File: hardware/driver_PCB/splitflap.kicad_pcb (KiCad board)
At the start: 2 copper layers, 111.8 x 95.2 mm, 19 parts, among them IC1 CD4049UBE, IC2 CD4049UBE, J1 Conn_01x02_Male, J2 Conn_01x08_Male, J3 Conn_01x16_Female, U1 74HC595, U2 74HC595, U3 SN754410NE, U4 SN754410NE, U5 SN754410NE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

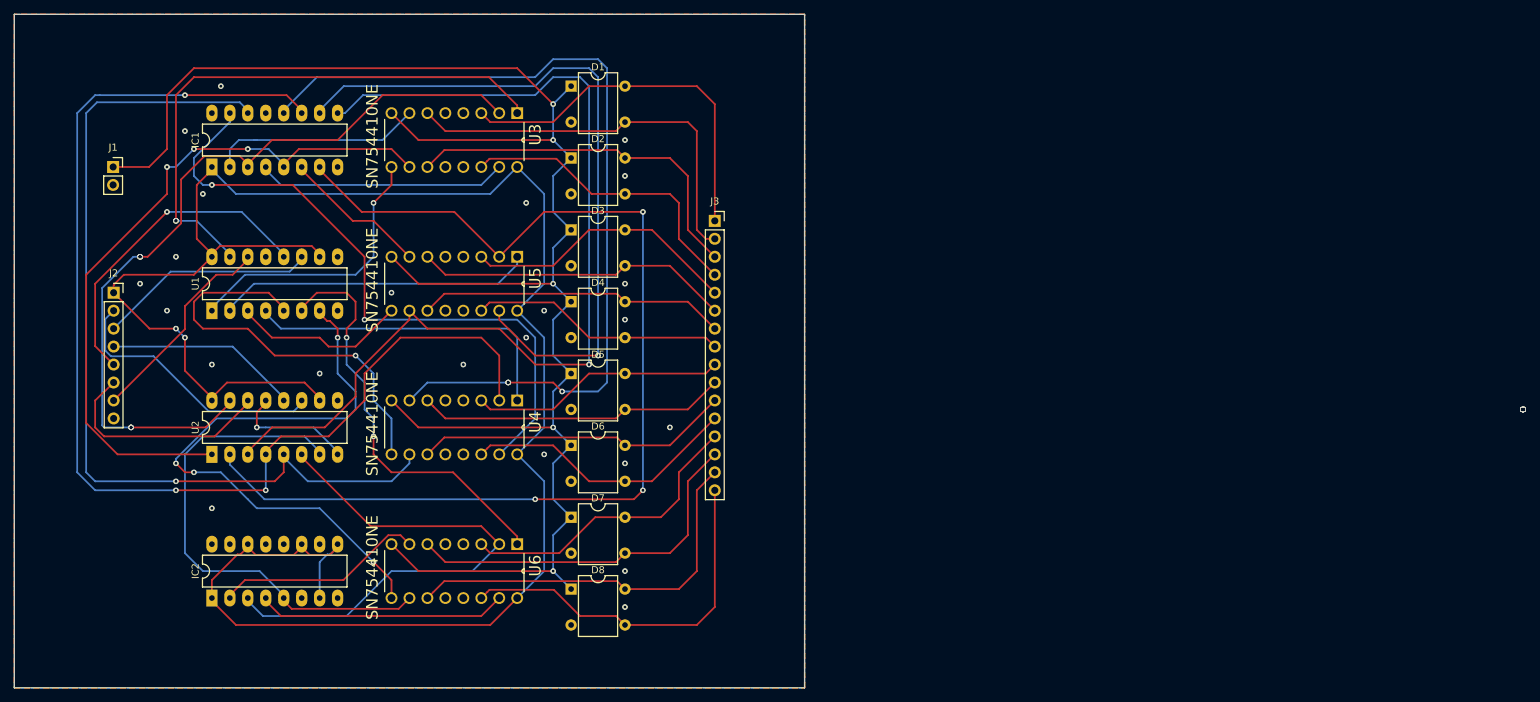
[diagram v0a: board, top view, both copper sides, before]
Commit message: changed pcb layout and interface
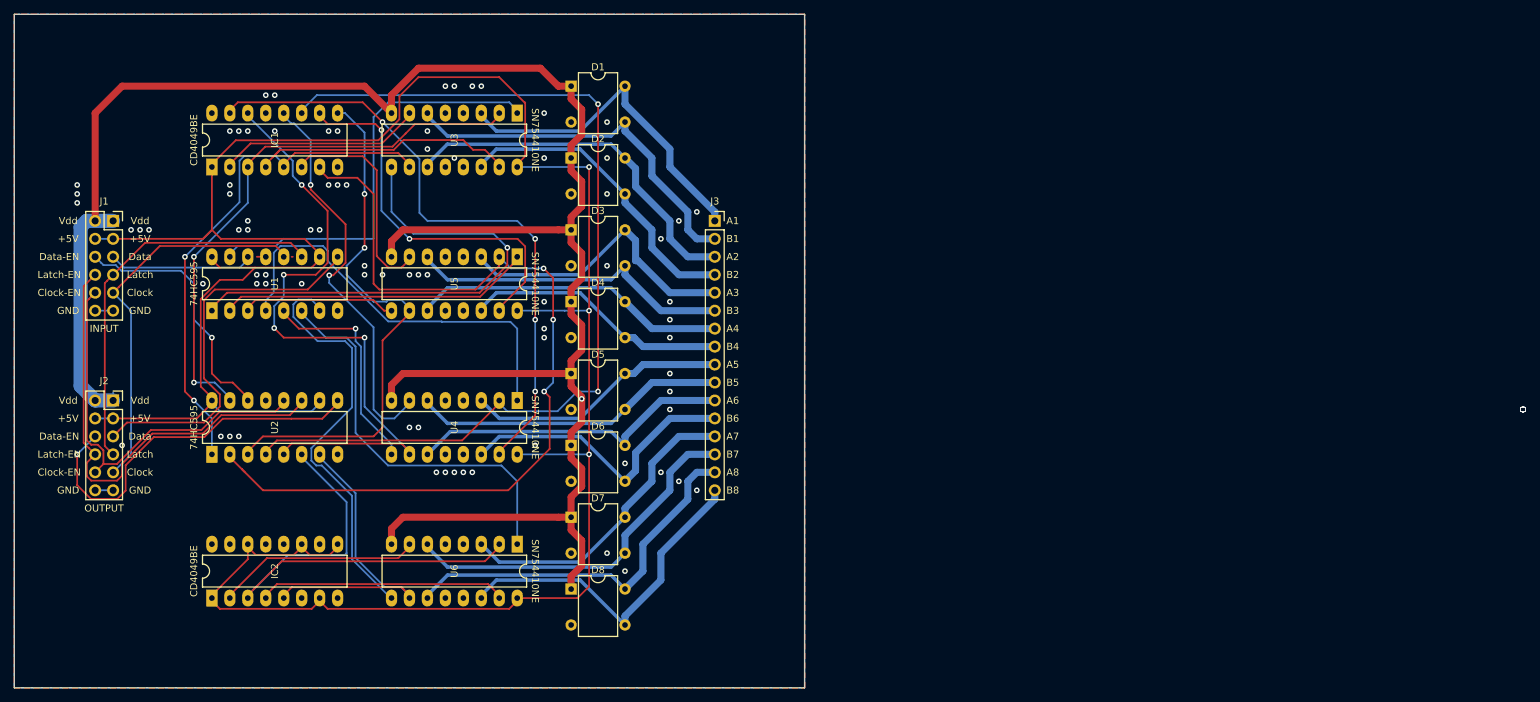
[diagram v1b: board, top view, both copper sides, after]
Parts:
- J1: value Conn_01x02_Male -> Conn_02x06_Odd_Even; footprint Connector_PinSocket_2.54mm:PinSocket_1x02_P2.54mm_Vertical -> Connector_PinSocket_2.54mm:PinSocket_2x06_P2.54mm_Vertical
- J2: value Conn_01x08_Male -> Conn_02x06_Odd_Even; footprint Connector_PinSocket_2.54mm:PinSocket_1x08_P2.54mm_Vertical -> Connector_PinSocket_2.54mm:PinSocket_2x06_P2.54mm_Vertical
- U3, U4, U5, U6: footprint CD4017BE:DIP254P762X508-16 -> Package_DIP:DIP-16_W7.62mm_LongPads
- moved U3 19.3 mm to (218.4, 39.4)
- moved U5 19.3 mm to (218.4, 59.7)
- moved U6 19.3 mm to (218.4, 100.3)
- moved U4 19.3 mm to (218.4, 80.0)
- moved J2 15.2 mm to (161.3, 80.0)
- moved J1 7.62 mm to (161.3, 54.6)
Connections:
- J1 pad 2: GND -> VDD
- J2 pad 1: VCC -> VDD
- J2 pad 2: Net-(J2-Pad2) -> VDD
- J2 pad 3: Net-(J2-Pad3) -> VCC
- J2 pad 4: Net-(J2-Pad4) -> VCC
- J2 pad 7: Net-(J2-Pad7) -> Net-(J1-Pad7)
- J2 pad 8: GND -> Net-(J1-Pad8)
- U1 pad 11: Net-(J2-Pad3) -> Net-(J1-Pad7)
- U1 pad 12: Net-(J2-Pad5) -> Net-(J1-Pad9)
- U1 pad 14: Net-(J2-Pad7) -> Net-(J1-Pad5)
- U1 pad 9: Net-(U1-Pad9) -> Net-(J2-Pad5)
- U2 pad 11: Net-(J2-Pad2) -> Net-(J1-Pad8)
- U2 pad 12: Net-(J2-Pad4) -> Net-(J1-Pad10)
- U2 pad 14: Net-(J2-Pad6) -> Net-(J1-Pad6)
- U2 pad 9: Net-(U2-Pad9) -> Net-(J2-Pad6)
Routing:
- net VCC: track 286.1 -> 356.1 mm, vias 2 -> 3
- net Net-(J1-Pad8): track 0.00 -> 66.9 mm
- net Net-(IC1-Pad12): track 124.1 -> 57.3 mm, vias 3 -> 2
- net Net-(IC1-Pad9): track 140.3 -> 76.5 mm, vias 1 -> 2
- net Net-(J1-Pad10): track 0.00 -> 57.3 mm
- net Net-(J1-Pad7): track 0.00 -> 56.1 mm
- net Net-(J1-Pad9): track 0.00 -> 55.2 mm
- net Net-(IC1-Pad10): track 99.5 -> 54.4 mm, vias 1 -> 2
- net Net-(J2-Pad2): track 38.3 -> 0.00 mm
- net Net-(J1-Pad6): track 0.00 -> 36.2 mm, vias 0 -> 1
- net Net-(IC1-Pad14): track 128.6 -> 93.8 mm, vias 1 -> 4
- net Net-(IC1-Pad3): track 112.9 -> 79.2 mm, vias 5 -> 2
- net Net-(U1-Pad1): track 40.0 -> 72.8 mm
- net VDD: track 258.2 -> 289.9 mm, vias 5 -> 1
- net Net-(J2-Pad3): track 31.0 -> 0.00 mm
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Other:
- net class Default: clearance 0.2 -> 0.25
- rule trace_clearance: 0.2 -> 0.25
- board text added: "+5V"
- board text added: "74HC595"
- board text added: "A1"
- board text added: "A2"
- board text added: "A3"
- board text added: "A4"
- board text added: "A5"
- board text added: "A6"
- board text added: "A7"
- board text added: "A8"
- board text added: "B1"
- board text added: "B2"
- board text added: "B3"
- board text added: "B4"
- board text added: "B5"
- board text added: "B6"
- board text added: "B7"
- board text added: "B8"
- board text added: "CD4049BE"
- board text added: "Clock"
- board text added: "Clock-EN"
- board text added: "Data"
- board text added: "Data-EN"
- board text added: "GND"
- board text added: "INPUT"
- board text added: "Latch"
- board text added: "Latch-EN"
- board text added: "OUTPUT"
- board text added: "SN754410NE"
- board text added: "Vdd"

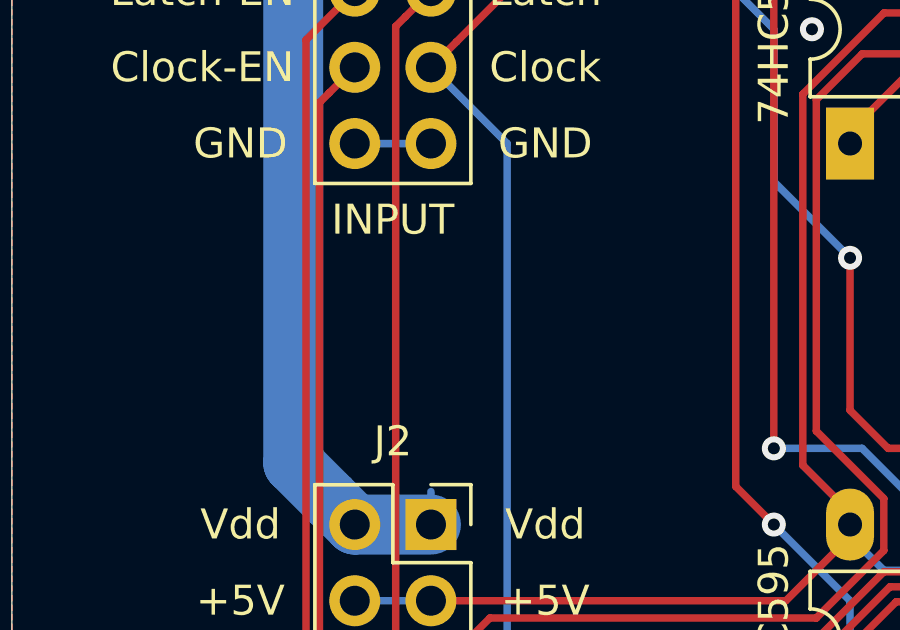
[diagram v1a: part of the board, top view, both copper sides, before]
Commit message: changed pcb layout and interface
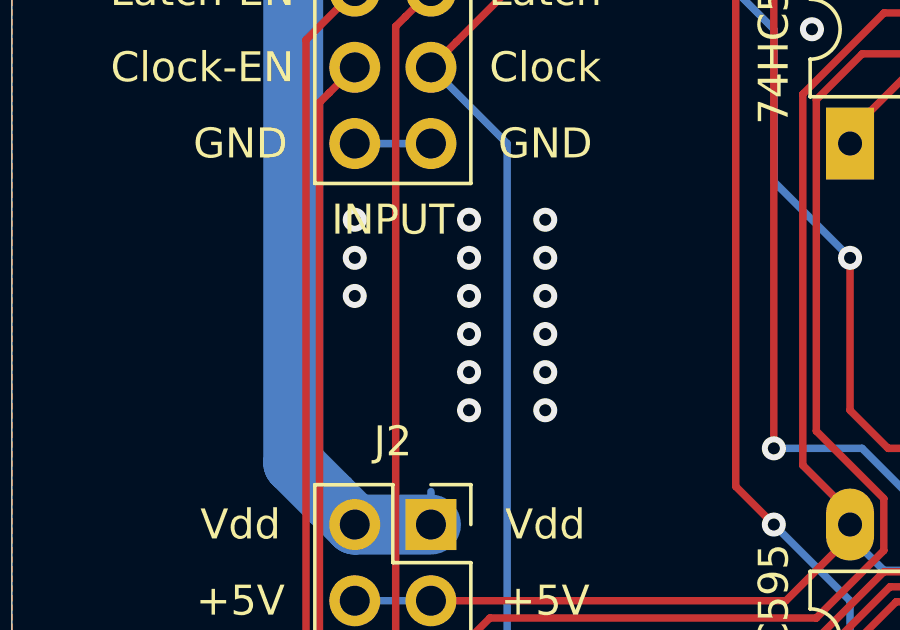
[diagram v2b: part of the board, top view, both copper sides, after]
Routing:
- net GND: vias 79 -> 94
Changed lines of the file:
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@@
     (thickness 1.6)
     (drawings 57)
-    (tracks 794)
+    (tracks 809)
     (zones 0)
     (modules 19)
@@
   (via (at 194.31 49.53) (size 0.8) (drill 0.4) (layers F.Cu B.Cu) (net 3))
   (via (at 196.85 60.96) (size 0.8) (drill 0.4) (layers F.Cu B.Cu) (net 3))
+  (via (at 162.56 69.85) (size 0.8) (drill 0.4) (layers F.Cu B.Cu) (net 3))
+  (via (at 162.56 71.12) (size 0.8) (drill 0.4) (layers F.Cu B.Cu) (net 3))
+  (via (at 162.56 72.39) (size 0.8) (drill 0.4) (layers F.Cu B.Cu) (net 3))
+  (via (at 162.56 73.66) (size 0.8) (drill 0.4) (layers F.Cu B.Cu) (net 3))
+  (via (at 162.56 74.93) (size 0.8) (drill 0.4) (layers F.Cu B.Cu) (net 3))
+  (via (at 162.56 76.2) (size 0.8) (drill 0.4) (layers F.Cu B.Cu) (net 3))
+  (via (at 165.1 69.85) (size 0.8) (drill 0.4) (layers F.Cu B.Cu) (net 3))
+  (via (at 165.1 71.12) (size 0.8) (drill 0.4) (layers F.Cu B.Cu) (net 3))
+  (via (at 165.1 72.39) (size 0.8) (drill 0.4) (layers F.Cu B.Cu) (net 3))
+  (via (at 165.1 73.66) (size 0.8) (drill 0.4) (layers F.Cu B.Cu) (net 3))
+  (via (at 165.1 74.93) (size 0.8) (drill 0.4) (layers F.Cu B.Cu) (net 3))
+  (via (at 165.1 76.2) (size 0.8) (drill 0.4) (layers F.Cu B.Cu) (net 3))
+  (via (at 158.75 69.85) (size 0.8) (drill 0.4) (layers F.Cu B.Cu) (net 3))
+  (via (at 158.75 71.12) (size 0.8) (drill 0.4) (layers F.Cu B.Cu) (net 3))
+  (via (at 158.75 72.39) (size 0.8) (drill 0.4) (layers F.Cu B.Cu) (net 3))
   (segment (start 246.38 53.34) (end 246.38 54.61) (width 1) (layer B.Cu) (net 4))
   (segment (start 240.03 46.99) (end 246.38 53.34) (width 1) (layer B.Cu) (net 4))
